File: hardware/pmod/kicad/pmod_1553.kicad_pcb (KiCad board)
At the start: 2 copper layers, 80 x 34.5 mm, 30 parts, among them IC1 TB001-500-02BE, IC2 TB001-500-02BE, J1 Conn_02x06_Top_Bottom, J2 Conn_01x02, J3 Conn_01x02, P1 78604-9JC, P2 78604-9JC, U2 VO2630, U3 VO2630

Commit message: updated schematic with output filter caps on recieve line. Added AFRL logo as a library so it won't get deleted.
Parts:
- added C5: 10pF, Capacitor_THT:C_Disc_D4.7mm_W2.5mm_P5.00mm, F.Cu at (108.5, 79.0)
- added C6: 10pF, Capacitor_THT:C_Disc_D4.7mm_W2.5mm_P5.00mm, F.Cu at (120.5, 83.0)
- added L1: afrl, logos:afrl, F.Cu at (150.5, 93.5)
- moved U3 4.00 mm to (131.3, 86.5)
- moved C8 4.00 mm to (125.0, 90.0)
- moved R3 4.00 mm to (143.0, 78.5)
- moved R4 4.00 mm to (143.0, 86.5)
- moved R10 0.50 mm to (117.0, 89.5)
- moved R9 0.50 mm to (113.5, 82.0)
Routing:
- net Net-(C5-Pad2): track 13.4 -> 20.1 mm
- net Net-(C6-Pad1): track 13.7 -> 18.3 mm
- net Net-(P2-Pad6): track 9.42 -> 5.42 mm
- net Net-(P2-Pad4): track 10.6 -> 7.93 mm
- net Net-(C7-Pad2): track 46.2 -> 43.8 mm
- net Net-(C4-Pad1): track 18.7 -> 19.3 mm

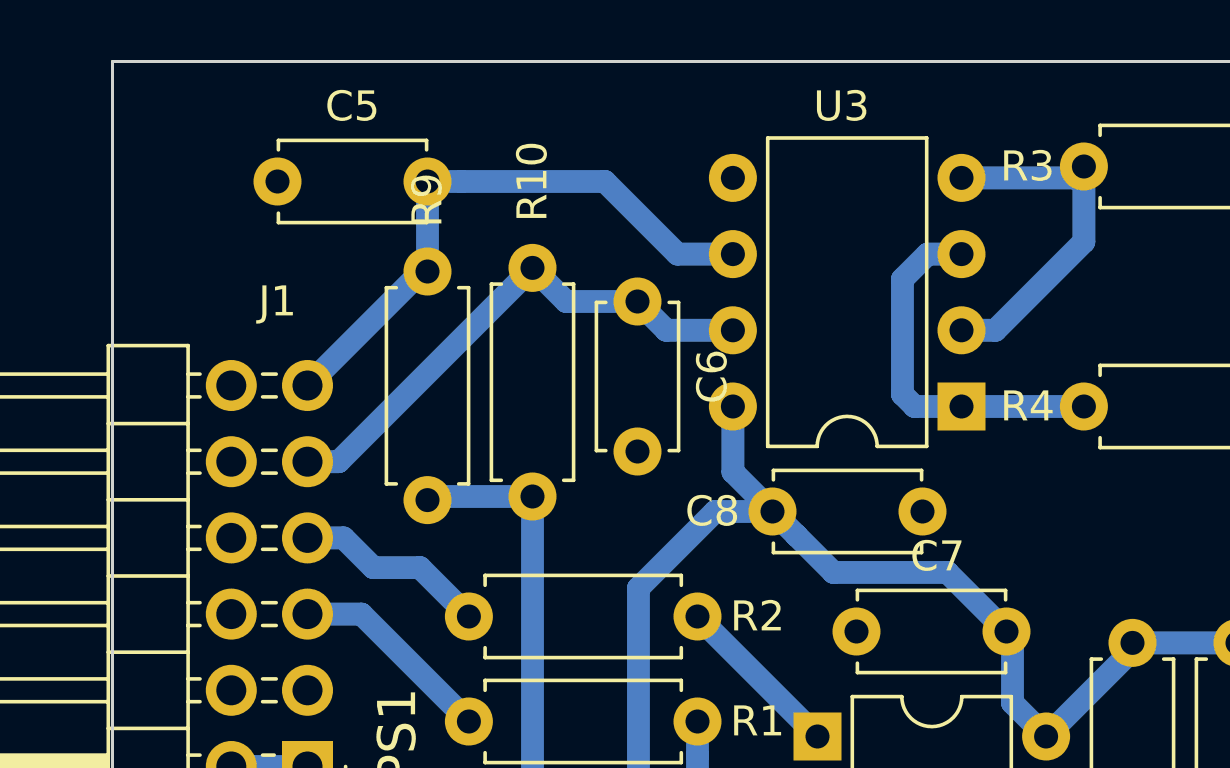
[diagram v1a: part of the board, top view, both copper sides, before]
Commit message: added testbench for fifos,they are barebones junk, but they are there and work with icarus.
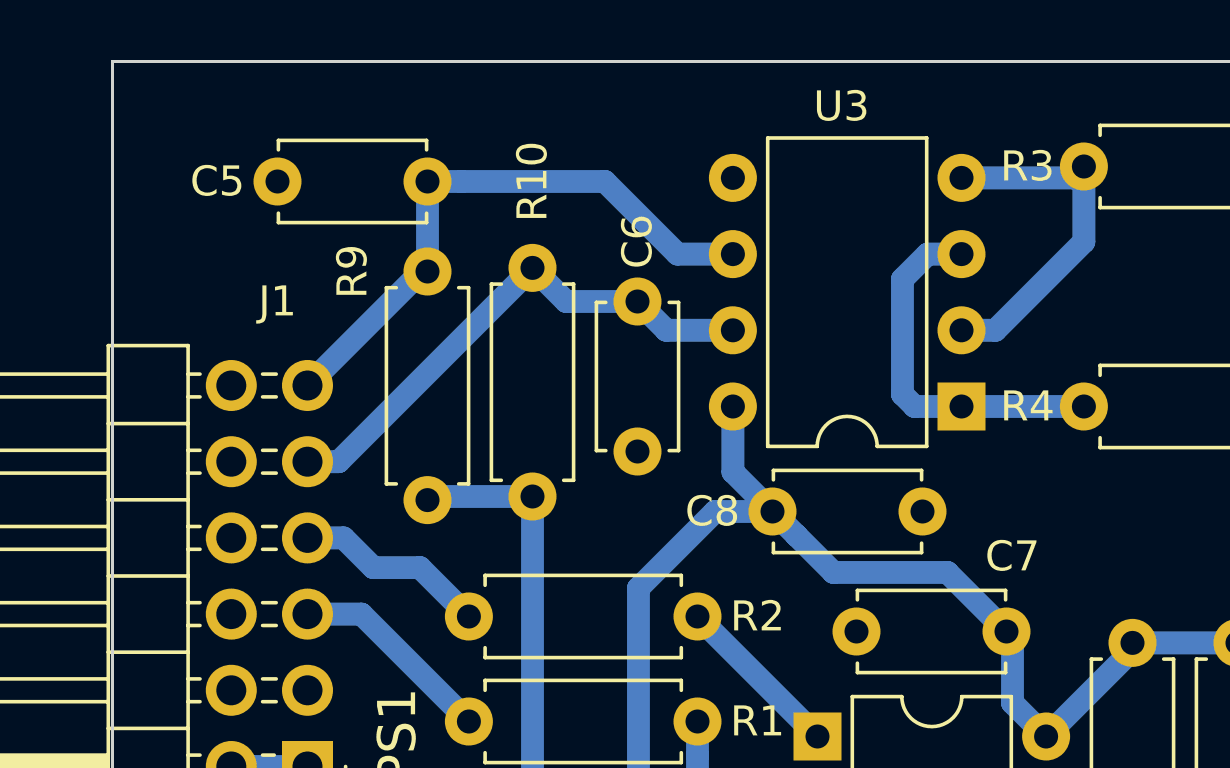
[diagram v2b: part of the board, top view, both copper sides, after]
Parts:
- C3, C4: value 22pF -> 10pF
- C5, C6: value 10pF -> 20pF
- R10, R9: value 2K2 -> 2K
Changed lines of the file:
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@@
     (descr "C, Disc series, Radial, pin pitch=5.00mm, , diameter*width=4.7*2.5mm^2, Capacitor, http://www.vishay.com/docs/45233/krseries.pdf")
     (tags "C Disc series Radial pin pitch 5.00mm  diameter 4.7mm width 2.5mm Capacitor")
-    (fp_text reference C6 (at 2.5 -2.5 90) (layer F.SilkS)
-      (effects (font (size 1 1) (thickness 0.15)))
-    )
-    (fp_text value 10pF (at 2.5 2.5 90) (layer F.Fab)
+    (fp_text reference C6 (at -2 0 90) (layer F.SilkS)
+      (effects (font (size 1 1) (thickness 0.15)))
+    )
+    (fp_text value 20pF (at 2.5 -1.5 90) (layer F.Fab)
       (effects (font (size 1 1) (thickness 0.15)))
     )
@@
     (descr "C, Disc series, Radial, pin pitch=5.00mm, , diameter*width=4.7*2.5mm^2, Capacitor, http://www.vishay.com/docs/45233/krseries.pdf")
     (tags "C Disc series Radial pin pitch 5.00mm  diameter 4.7mm width 2.5mm Capacitor")
-    (fp_text reference C5 (at 2.5 -2.5) (layer F.SilkS)
-      (effects (font (size 1 1) (thickness 0.15)))
-    )
-    (fp_text value 10pF (at 2.5 2.5) (layer F.Fab)
+    (fp_text reference C5 (at -2 0) (layer F.SilkS)
+      (effects (font (size 1 1) (thickness 0.15)))
+    )
+    (fp_text value 20pF (at 2.5 2.5) (layer F.Fab)
       (effects (font (size 1 1) (thickness 0.15)))
     )
@@
     (descr "C, Disc series, Radial, pin pitch=5.00mm, , diameter*width=4.7*2.5mm^2, Capacitor, http://www.vishay.com/docs/45233/krseries.pdf")
     (tags "C Disc series Radial pin pitch 5.00mm  diameter 4.7mm width 2.5mm Capacitor")
-    (fp_text reference C7 (at 2.7 -2.5) (layer F.SilkS)
+    (fp_text reference C7 (at 5.2 -2.5) (layer F.SilkS)
       (effects (font (size 1 1) (thickness 0.15)))
     )
@@
       (effects (font (size 1 1) (thickness 0.15)))
     )
-    (fp_text value 22pF (at 2.5 2.5 90) (layer F.Fab)
+    (fp_text value 10pF (at 2.5 2.5 90) (layer F.Fab)
       (effects (font (size 1 1) (thickness 0.15)))
     )
@@
       (effects (font (size 1 1) (thickness 0.15)))
     )
-    (fp_text value 22pF (at 2.5 2.5 90) (layer F.Fab)
+    (fp_text value 10pF (at 2.5 2.5 90) (layer F.Fab)
       (effects (font (size 1 1) (thickness 0.15)))
     )
@@
       (effects (font (size 1 1) (thickness 0.15)))
     )
-    (fp_text value 2K2 (at 3.81 2.37 90) (layer F.Fab)
+    (fp_text value 2K (at 3.81 2.37 90) (layer F.Fab)
       (effects (font (size 1 1) (thickness 0.15)))
     )
@@
     (descr "Resistor, Axial_DIN0207 series, Axial, Horizontal, pin pitch=7.62mm, 0.25W = 1/4W, length*diameter=6.3*2.5mm^2, http://cdn-reichelt.de/documents/datenblatt/B400/1_4W%23YAG.pdf")
     (tags "Resistor Axial_DIN0207 series Axial Horizontal pin pitch 7.62mm 0.25W = 1/4W length 6.3mm diameter 2.5mm")
-    (fp_text reference R9 (at -2.38 0 90) (layer F.SilkS)
-      (effects (font (size 1 1) (thickness 0.15)))
-    )
-    (fp_text value 2K2 (at 3.81 2.37 90) (layer F.Fab)
+    (fp_text reference R9 (at 0 2.5 90) (layer F.SilkS)
+      (effects (font (size 1 1) (thickness 0.15)))
+    )
+    (fp_text value 2K (at 3.81 2.37 90) (layer F.Fab)
       (effects (font (size 1 1) (thickness 0.15)))
     )
@@
   (segment (start 111.3 93.42) (end 109.5 93.42) (width 0.762) (layer B.Cu) (net 14))
   (segment (start 114.88 97) (end 111.3 93.42) (width 0.762) (layer B.Cu) (net 14))
-  (segment (start 109.5 85.8) (end 109.5 85.5) (width 0.762) (layer B.Cu) (net 31))
-  (segment (start 110.04 88.34) (end 109.5 88.34) (width 0.762) (layer B.Cu) (net 32))
   (segment (start 162 101.54) (end 162.04 101.5) (width 0.762) (layer B.Cu) (net 17))
   (segment (start 162.46 101.54) (end 162.5 101.5) (width 0.762) (layer B.Cu) (net 17))
@@
   (segment (start 130.16863 81.42) (end 131.3 81.42) (width 0.762) (layer B.Cu) (net 30))
   (segment (start 131.3 86.5) (end 129.738 86.5) (width 0.762) (layer B.Cu) (net 30))
+  (segment (start 109.5 85.8) (end 109.5 85.5) (width 0.762) (layer B.Cu) (net 31))
   (segment (start 113.3 82) (end 109.5 85.8) (width 0.762) (layer B.Cu) (net 31))
   (segment (start 113.5 82) (end 113.3 82) (width 0.762) (layer B.Cu) (net 31))
@@
   (segment (start 121.833234 81.42) (end 119.413234 79) (width 0.762) (layer B.Cu) (net 31))
   (segment (start 123.68 81.42) (end 121.833234 81.42) (width 0.762) (layer B.Cu) (net 31))
+  (segment (start 110.04 88.34) (end 109.5 88.34) (width 0.762) (layer B.Cu) (net 32))
   (segment (start 121.46 83.96) (end 120.5 83) (width 0.762) (layer B.Cu) (net 32))
   (segment (start 123.68 83.96) (end 121.46 83.96) (width 0.762) (layer B.Cu) (net 32))

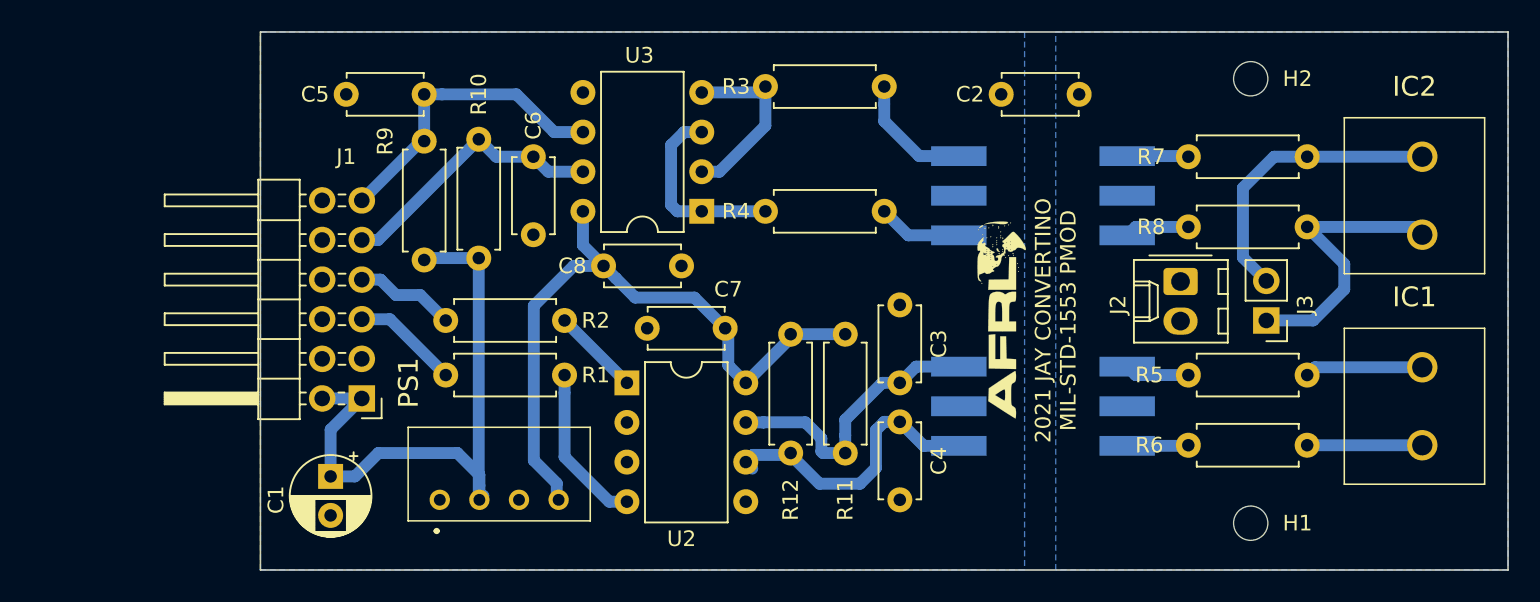
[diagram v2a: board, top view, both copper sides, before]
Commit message: added 1553 to fmc1553 core, need adc/dac interface connection. added arty mcs file.
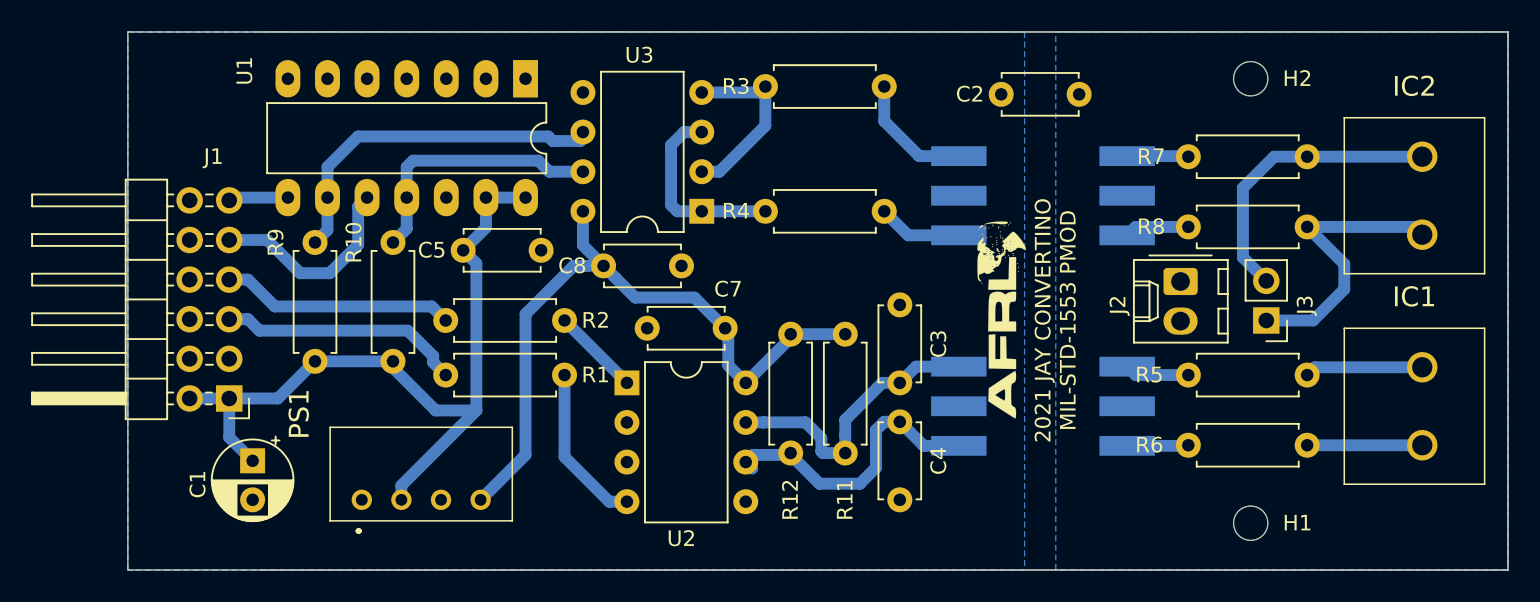
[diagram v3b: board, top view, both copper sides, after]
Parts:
- removed C6: 20pF, Capacitor_THT:C_Disc_D4.7mm_W2.5mm_P5.00mm
- added U1: 74HC14, Package_DIP:DIP-14_W7.62mm_LongPads, F.Cu at (120.0, 78.0)
- C5: value 20pF -> 100NF
- R10, R9: value 2K -> 330
- moved C5 16.0 mm to (121.0, 89.0), turned to 180 degrees
- moved R9 9.55 mm to (106.5, 88.5)
- moved R10 8.61 mm to (111.5, 96.1)
- moved J1 8.50 mm to (101.0, 98.5)
- moved C1 5.10 mm to (102.5, 102.5)
- moved PS1 5.00 mm to (109.5, 105.0)
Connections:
- C5 pad 2: Net-(C5-Pad2) -> Net-(C1-Pad1)
- J1 pad 11: Net-(C5-Pad2) -> Net-(J1-Pad11)
- J1 pad 9: Net-(C6-Pad1) -> Net-(J1-Pad9)
- R10 pad 2: Net-(C6-Pad1) -> Net-(R10-Pad2)
- R9 pad 1: Net-(C5-Pad2) -> Net-(R9-Pad1)
- U3 pad 6: Net-(C5-Pad2) -> Net-(R9-Pad1)
- U3 pad 7: Net-(C6-Pad1) -> Net-(R10-Pad2)
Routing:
- net Net-(R9-Pad1): track 0.00 -> 23.0 mm
- net Net-(C5-Pad2): track 20.1 -> 0.00 mm
- net Net-(C6-Pad1): track 18.3 -> 0.00 mm
- net Net-(R10-Pad2): track 0.00 -> 17.0 mm
- net Net-(J1-Pad9): track 0.00 -> 13.2 mm
- net Net-(C1-Pad1): track 40.8 -> 51.2 mm
- net Net-(J1-Pad5): track 6.86 -> 15.6 mm
- net Net-(J1-Pad7): track 6.47 -> 15.0 mm
- net Net-(J1-Pad11): track 0.00 -> 3.83 mm
- net Net-(C7-Pad2): track 43.8 -> 44.6 mm
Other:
- board size 80 x 34.5 mm -> 88.5 x 34.5 mm

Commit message: added documents for linux build, dac switch added, and pcb has small updates.
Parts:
- added C6: 22pF_DNP, Capacitor_THT:C_Disc_D4.7mm_W2.5mm_P5.00mm, F.Cu at (107.5, 82.5)
- added C9: 22pF_DNP, Capacitor_THT:C_Disc_D4.7mm_W2.5mm_P5.00mm, F.Cu at (120.0, 83.0)
- R10, R9: value 330 -> 330_2K2-DNP
